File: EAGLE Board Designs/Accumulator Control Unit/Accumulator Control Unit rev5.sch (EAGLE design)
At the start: 254 parts, among them J1 CONNECTOR-12_MF_T_V_, J2 CONNECTOR-6_μF_T_V_BLACK, J3 CONNECTOR-4_μF_T_V_BLACK, J4 CONNECTOR-2_MF_T_V_, J5 CONNECTOR-8_μF_T_V_BLACK, J6 CONNECTOR-14_MF_T_V_, J7 JUMPER__1X02, J8 JUMPER__1X02, J9 CONNECTOR-2_MF_T_V_, Q1 TRANSISTOR_N_MOS__PMV15ENEA, Q2 TRANSISTOR_N_MOS__PMV15ENEA, Q3 TRANSISTOR_N_MOS__PMV15ENEA, Q4 TRANSISTOR_N_MOS__PMV15ENEA, T1 TRANSFORMER_HM2112ZNLT_AIRGAP, T2 TRANSFORMER_HM2112ZNLT_AIRGAP, U1 VOLTAGE_REGULATOR_SOT-223_3.3V, U10 TCAN1051HQV-Q1, U11 OPAMP_1_CHANNEL_OPA991, U12 OPAMP_1_CHANNEL_OPA991, U13 OPAMP_1_CHANNEL_OPA991, U14 RELAY_SOLIDSTATE_NO_DIP-4, U15 LM555, U16 OPAMP_1_CHANNEL_OPA991, U17 MAX7404, U18 OPAMP_1_CHANNEL_OPA991, U19 MAX7404, U2 RELAY_SOLIDSTATE_NO_DIP-4, U20 LOGICGATE_BUFFER, U21 ADM8316WBX30, U22 OPAMP_1_CHANNEL_OPA991, U23 LOGICGATE_AND_DCK3, U24 LOGICGATE_AND_DCK3, U25 LOGICGATE_AND_DCK3, U26 OPAMP_1_CHANNEL_OPA991, U27 ADG1423, U28 OPAMP_1_CHANNEL_OPA991, U29 MAX7404, U3 RELAY_SOLIDSTATE_NO_DIP-4, U30 OPAMP_1_CHANNEL_OPA991, U31 MAX7404, U32 LTC6820, U4 OPAMP_1_CHANNEL_OPA991, U5 OPAMP_1_CHANNEL_OPA991, U6 TCAN1051HQV-Q1, U7 LTC6820, U8 OPAMP_1_CHANNEL_OPA991, U9 OPAMP_1_CHANNEL_OPA991

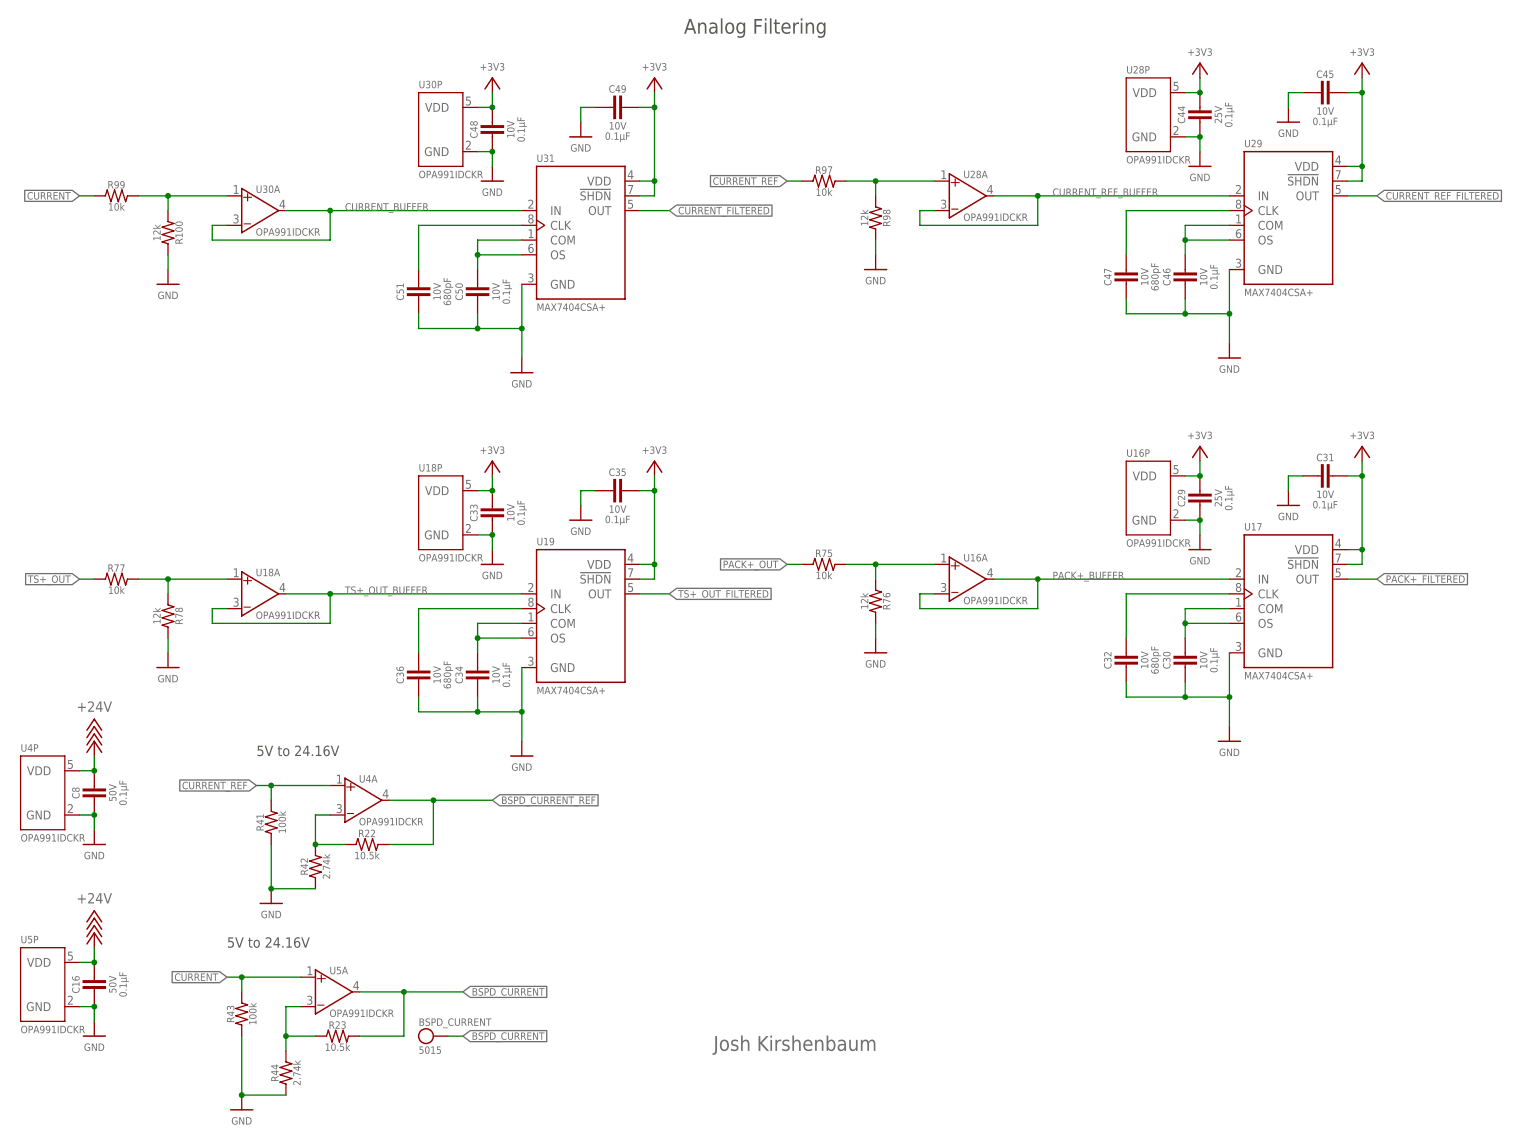
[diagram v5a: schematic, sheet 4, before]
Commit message: changes to resistors
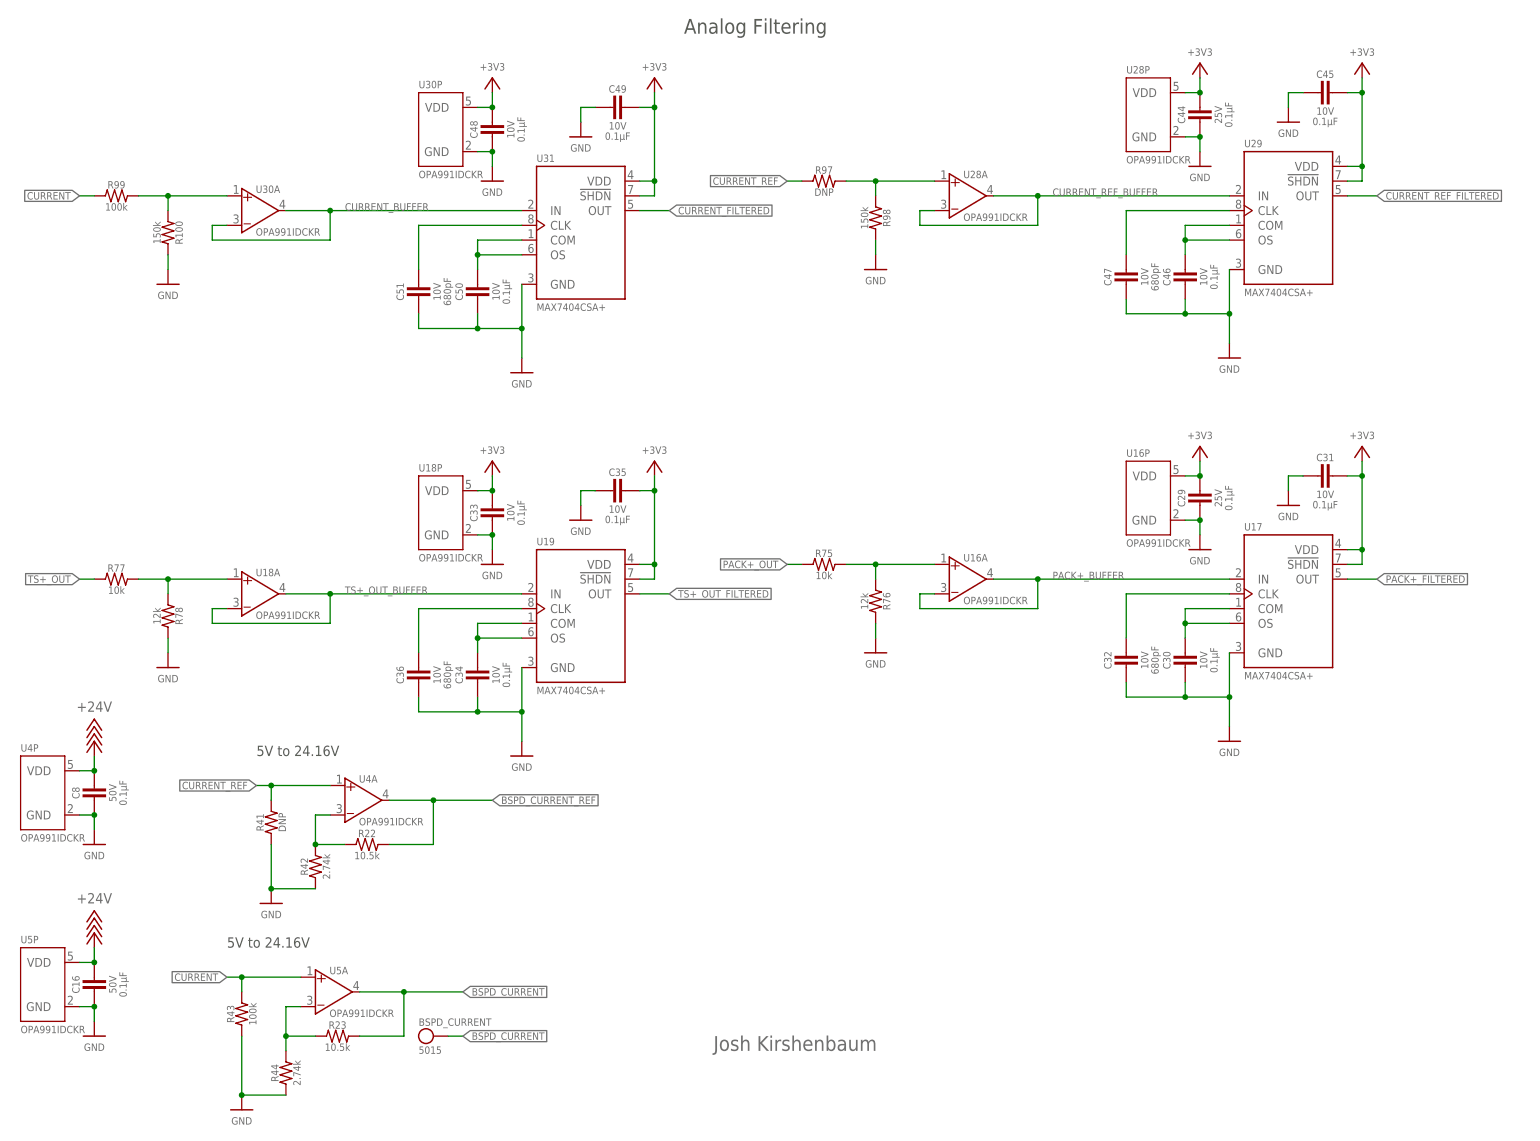
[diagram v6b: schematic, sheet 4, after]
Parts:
- R100, R98: value RESISTOR_0603_12K -> RESISTOR_0603_150K; device HyTechDevices - Copy:RESISTOR_0603_12K -> HyTechDevices:RESISTOR_0603_150K
- R103, R30: value RESISTOR_0603_1K -> RESISTOR_0603_1.65K; device HyTechDevices - Copy:RESISTOR_0603_1K -> HyTechDevices:RESISTOR_0603_1.65K
- R104, R31: value RESISTOR_0603_1K -> RESISTOR_0603_470; device HyTechDevices - Copy:RESISTOR_0603_1K -> HyTechDevices:RESISTOR_0603_470
- R41: value RESISTOR_0603_100K -> RESISTOR_0603_DNP; device HyTechDevices:RESISTOR_0603_100K -> HyTechDevices:RESISTOR_0603_DNP
- R53: value RESISTOR_0603_11.5K -> RESISTOR_0603_5.9K; device HyTechDevices:RESISTOR_0603_11.5K -> HyTechDevices:RESISTOR_0603_5.9K
- R54: value RESISTOR_0603_5.9K -> RESISTOR_0603_11.5K; device HyTechDevices:RESISTOR_0603_5.9K -> HyTechDevices:RESISTOR_0603_11.5K
- R97: value RESISTOR_0603_10K -> RESISTOR_0603_DNP; device HyTechDevices - Copy:RESISTOR_0603_10K -> HyTechDevices:RESISTOR_0603_DNP
- R99: value RESISTOR_0603_10K -> RESISTOR_0603_100K; device HyTechDevices - Copy:RESISTOR_0603_10K -> HyTechDevices:RESISTOR_0603_100K
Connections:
- removed net INVERTER_24V: J1.1
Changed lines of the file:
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@@
 <part name="GND17" library="HyTechSupplies" deviceset="GND" device=""/>
 <part name="P+9" library="HyTechSupplies" deviceset="+5V" device=""/>
-<part name="R54" library="HyTechDevices" deviceset="RESISTOR_?_*" device="0603" technology="5.9K" value="RESISTOR_0603_5.9K"/>
-<part name="R53" library="HyTechDevices" deviceset="RESISTOR_?_*" device="0603" technology="11.5K"/>
+<part name="R54" library="HyTechDevices" deviceset="RESISTOR_?_*" device="0603" technology="11.5K" value="RESISTOR_0603_11.5K"/>
+<part name="R53" library="HyTechDevices" deviceset="RESISTOR_?_*" device="0603" technology="5.9K" value="RESISTOR_0603_5.9K"/>
 <part name="GND20" library="HyTechSupplies" deviceset="GND" device=""/>
 <part name="P+10" library="HyTechSupplies" deviceset="+5V" device=""/>
@@
 <part name="P72" library="HyTechSupplies" deviceset="+3V3" device=""/>
 <part name="P73" library="HyTechSupplies" deviceset="GND" device=""/>
-<part name="R30" library="HyTechDevices - Copy" deviceset="RESISTOR_?_*" device="0603" technology="1K"/>
-<part name="R31" library="HyTechDevices - Copy" deviceset="RESISTOR_?_*" device="0603" technology="1K"/>
+<part name="R30" library="HyTechDevices" deviceset="RESISTOR_?_*" device="0603" technology="1.65K" value="RESISTOR_0603_1.65K"/>
+<part name="R31" library="HyTechDevices" deviceset="RESISTOR_?_*" device="0603" technology="470" value="RESISTOR_0603_470"/>
 <part name="P74" library="HyTechSupplies" deviceset="GND" device=""/>
 <part name="T1" library="HyTechDevices" deviceset="TRANSFORMER" device="_HM2112ZNLT_AIRGAP"/>
@@
 <part name="P78" library="HyTechSupplies" deviceset="GND" device=""/>
 <part name="C51" library="HyTechDevices - Copy" deviceset="CAPACITOR_?_*" device="0603" technology="10V_680PF"/>
-<part name="R99" library="HyTechDevices - Copy" deviceset="RESISTOR_?_*" device="0603" technology="10K"/>
-<part name="R100" library="HyTechDevices - Copy" deviceset="RESISTOR_?_*" device="0603" technology="12K"/>
+<part name="R99" library="HyTechDevices" deviceset="RESISTOR_?_*" device="0603" technology="100K" value="RESISTOR_0603_100K"/>
+<part name="R100" library="HyTechDevices" deviceset="RESISTOR_?_*" device="0603" technology="150K" value="RESISTOR_0603_150K"/>
 <part name="P81" library="HyTechSupplies" deviceset="GND" device=""/>
 <part name="P88" library="HyTechSupplies" deviceset="+3V3" device=""/>
@@
 <part name="P92" library="HyTechSupplies" deviceset="GND" device=""/>
 <part name="C47" library="HyTechDevices - Copy" deviceset="CAPACITOR_?_*" device="0603" technology="10V_680PF"/>
-<part name="R97" library="HyTechDevices - Copy" deviceset="RESISTOR_?_*" device="0603" technology="10K"/>
-<part name="R98" library="HyTechDevices - Copy" deviceset="RESISTOR_?_*" device="0603" technology="12K"/>
+<part name="R97" library="HyTechDevices" deviceset="RESISTOR_?_*" device="0603" technology="DNP" value="RESISTOR_0603_DNP"/>
+<part name="R98" library="HyTechDevices" deviceset="RESISTOR_?_*" device="0603" technology="150K" value="RESISTOR_0603_150K"/>
 <part name="P93" library="HyTechSupplies" deviceset="GND" device=""/>
 <part name="P94" library="HyTechSupplies" deviceset="+3V3" device=""/>
@@
 <part name="P38" library="HyTechSupplies" deviceset="GND" device=""/>
 <part name="C8" library="HyTechDevices" deviceset="CAPACITOR_?_*" device="0603" technology="50V_0.1UF" value="CAPACITOR_0603_50V_0.1UF"/>
-<part name="R41" library="HyTechDevices" deviceset="RESISTOR_?_*" device="0603" technology="100K" value="RESISTOR_0603_100K"/>
+<part name="R41" library="HyTechDevices" deviceset="RESISTOR_?_*" device="0603" technology="DNP" value="RESISTOR_0603_DNP"/>
 <part name="P70" library="HyTechSupplies" deviceset="GND" device=""/>
 <part name="R42" library="HyTechDevices" deviceset="RESISTOR_?_*" device="0603" technology="2.74K" value="RESISTOR_0603_2.74K"/>
@@
 <part name="P127" library="HyTechSupplies" deviceset="+3V3" device=""/>
 <part name="C53" library="HyTechDevices" deviceset="CAPACITOR_?_*" device="0603" technology="10V_0.1UF"/>
-<part name="R103" library="HyTechDevices - Copy" deviceset="RESISTOR_?_*" device="0603" technology="1K"/>
-<part name="R104" library="HyTechDevices - Copy" deviceset="RESISTOR_?_*" device="0603" technology="1K"/>
+<part name="R103" library="HyTechDevices" deviceset="RESISTOR_?_*" device="0603" technology="1.65K" value="RESISTOR_0603_1.65K"/>
+<part name="R104" library="HyTechDevices" deviceset="RESISTOR_?_*" device="0603" technology="470" value="RESISTOR_0603_470"/>
 <part name="P128" library="HyTechSupplies" deviceset="GND" device=""/>
 <part name="T2" library="HyTechDevices" deviceset="TRANSFORMER" device="_HM2112ZNLT_AIRGAP"/>
@@
 </segment>
 </net>
-<net name="INVERTER_24V" class="0">
-<segment>
-<pinref part="J1" gate="G$1" pin="1"/>
-<wire x1="20.32" y1="124.46" x2="45.72" y2="124.46" width="0.1524" layer="91"/>
-<label x="45.72" y="124.46" size="1.27" layer="95" xref="yes"/>
-</segment>
-</net>
